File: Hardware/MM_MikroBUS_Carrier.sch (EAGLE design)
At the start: 52 parts, among them J15 MICROMOD-2222-C, J2 QWIIC_RIGHT_ANGLE, J5 Vertical Qwiic Connector, J7 MIKROBUS_SMD_BLACK1, J9 CORTEX_JTAG_DEBUG_MINIMUM_PTH, U1 MCP73831, U2 AP7361C-33FGEUDFN-8

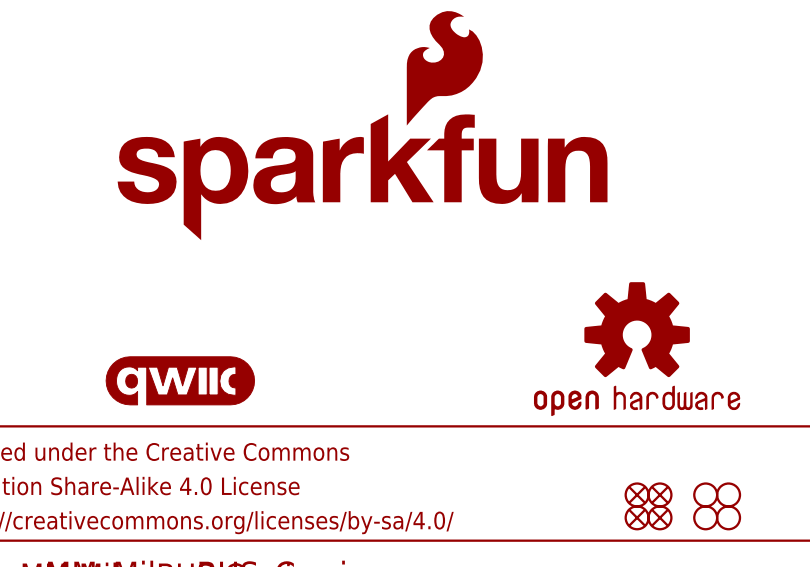
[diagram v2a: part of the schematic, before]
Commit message: Design review updates:
* Put mikroBUS pin labels into the table
* Add y-measure for mikroBUS socket
* Add mikroBUS logo to library and to the back of the board
* Add GND vias
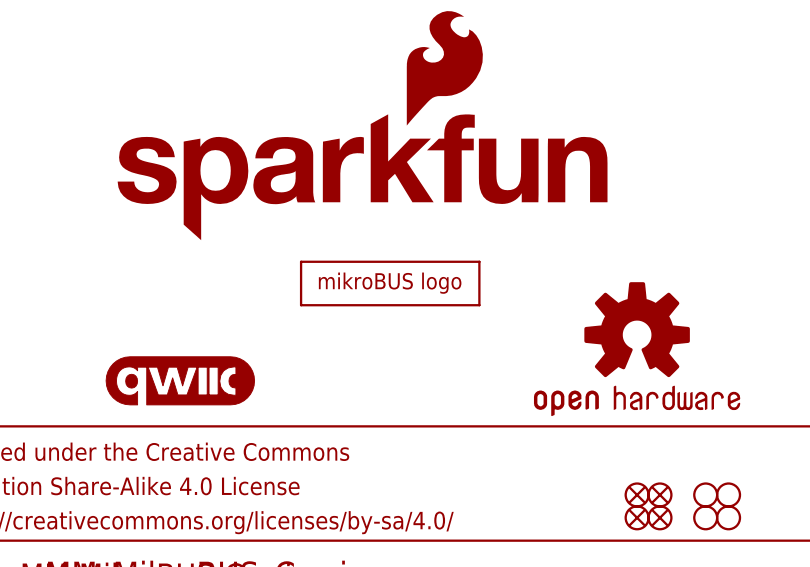
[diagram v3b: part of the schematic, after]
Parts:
- added U$7: MIKROBUS_LOGO, mikroBUS_SMD_BLACK:MIKROBUS_LOGO
- SWDCK, SWDIO: value TEST-POINT3 -> TEST-POINTTP_15TH_THRU; device SparkFun-Connectors:TEST-POINT3 -> SparkFun-Connectors:TEST-POINTTP_15TH_THRU
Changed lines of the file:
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@@
 <grid distance="0.1" unitdist="inch" unit="inch" style="lines" multiple="1" display="no" altdistance="0.01" altunitdist="inch" altunit="inch"/>
 <layers>
-<layer number="1" name="Top" color="4" fill="1" visible="no" active="no"/>
-<layer number="2" name="Route2" color="1" fill="3" visible="no" active="no"/>
-<layer number="3" name="Route3" color="4" fill="3" visible="no" active="no"/>
-<layer number="4" name="Route4" color="1" fill="4" visible="no" active="no"/>
-<layer number="5" name="Route5" color="4" fill="4" visible="no" active="no"/>
-<layer number="6" name="Route6" color="1" fill="8" visible="no" active="no"/>
-<layer number="7" name="Route7" color="4" fill="8" visible="no" active="no"/>
-<layer number="8" name="Route8" color="1" fill="2" visible="no" active="no"/>
-<layer number="9" name="Route9" color="4" fill="2" visible="no" active="no"/>
-<layer number="10" name="Route10" color="1" fill="7" visible="no" active="no"/>
-<layer number="11" name="Route11" color="4" fill="7" visible="no" active="no"/>
-<layer number="12" name="Route12" color="1" fill="5" visible="no" active="no"/>
-<layer number="13" name="Route13" color="4" fill="5" visible="no" active="no"/>
-<layer number="14" name="Route14" color="1" fill="6" visible="no" active="no"/>
-<layer number="15" name="Route15" color="4" fill="6" visible="no" active="no"/>
-<layer number="16" name="Bottom" color="1" fill="1" visible="no" active="no"/>
-<layer number="17" name="Pads" color="2" fill="1" visible="no" active="no"/>
-<layer number="18" name="Vias" color="2" fill="1" visible="no" active="no"/>
-<layer number="19" name="Unrouted" color="6" fill="1" visible="no" active="no"/>
-<layer number="20" name="Dimension" color="24" fill="1" visible="no" active="no"/>
-<layer number="21" name="tPlace" color="16" fill="1" visible="no" active="no"/>
-<layer number="22" name="bPlace" color="14" fill="1" visible="no" active="no"/>
-<layer number="23" name="tOrigins" color="15" fill="1" visible="no" active="no"/>
-<layer number="24" name="bOrigins" color="15" fill="1" visible="no" active="no"/>
-<layer number="25" name="tNames" color="7" fill="1" visible="no" active="no"/>
-<layer number="26" name="bNames" color="7" fill="1" visible="no" active="no"/>
-<layer number="27" name="tValues" color="7" fill="1" visible="no" active="no"/>
-<layer number="28" name="bValues" color="7" fill="1" visible="no" active="no"/>
+<layer number="1" name="Top" color="4" fill="1" visible="yes" active="no"/>
+<layer number="2" name="Route2" color="1" fill="3" visible="yes" active="no"/>
+<layer number="3" name="Route3" color="4" fill="3" visible="yes" active="no"/>
+<layer number="4" name="Route4" color="1" fill="4" visible="yes" active="no"/>
+<layer number="5" name="Route5" color="4" fill="4" visible="yes" active="no"/>
+<layer number="6" name="Route6" color="1" fill="8" visible="yes" active="no"/>
+<layer number="7" name="Route7" color="4" fill="8" visible="yes" active="no"/>
+<layer number="8" name="Route8" color="1" fill="2" visible="yes" active="no"/>
+<layer number="9" name="Route9" color="4" fill="2" visible="yes" active="no"/>
+<layer number="10" name="Route10" color="1" fill="7" visible="yes" active="no"/>
+<layer number="11" name="Route11" color="4" fill="7" visible="yes" active="no"/>
+<layer number="12" name="Route12" color="1" fill="5" visible="yes" active="no"/>
+<layer number="13" name="Route13" color="4" fill="5" visible="yes" active="no"/>
+<layer number="14" name="Route14" color="1" fill="6" visible="yes" active="no"/>
+<layer number="15" name="Route15" color="4" fill="6" visible="yes" active="no"/>
+<layer number="16" name="Bottom" color="1" fill="1" visible="yes" active="no"/>
+<layer number="17" name="Pads" color="2" fill="1" visible="yes" active="no"/>
+<layer number="18" name="Vias" color="2" fill="1" visible="yes" active="no"/>
+<layer number="19" name="Unrouted" color="6" fill="1" visible="yes" active="no"/>
+<layer number="20" name="Dimension" color="24" fill="1" visible="yes" active="no"/>
+<layer number="21" name="tPlace" color="16" fill="1" visible="yes" active="no"/>
+<layer number="22" name="bPlace" color="14" fill="1" visible="yes" active="no"/>
+<layer number="23" name="tOrigins" color="15" fill="1" visible="yes" active="no"/>
+<layer number="24" name="bOrigins" color="15" fill="1" visible="yes" active="no"/>
+<layer number="25" name="tNames" color="7" fill="1" visible="yes" active="no"/>
+<layer number="26" name="bNames" color="7" fill="1" visible="yes" active="no"/>
+<layer number="27" name="tValues" color="7" fill="1" visible="yes" active="no"/>
+<layer number="28" name="bValues" color="7" fill="1" visible="yes" active="no"/>
 <layer number="29" name="tStop" color="7" fill="3" visible="no" active="no"/>
 <layer number="30" name="bStop" color="7" fill="6" visible="no" active="no"/>
@@
 <layer number="35" name="tGlue" color="7" fill="4" visible="no" active="no"/>
 <layer number="36" name="bGlue" color="7" fill="5" visible="no" active="no"/>
-<layer number="37" name="tTest" color="7" fill="1" visible="no" active="no"/>
-<layer number="38" name="bTest" color="7" fill="1" visible="no" active="no"/>
+<layer number="37" name="tTest" color="7" fill="1" visible="yes" active="no"/>
+<layer number="38" name="bTest" color="7" fill="1" visible="yes" active="no"/>
 <layer number="39" name="tKeepout" color="4" fill="11" visible="no" active="no"/>
 <layer number="40" name="bKeepout" color="1" fill="11" visible="no" active="no"/>
@@
 <layer number="44" name="Drills" color="7" fill="1" visible="no" active="no"/>
 <layer number="45" name="Holes" color="7" fill="1" visible="no" active="no"/>
-<layer number="46" name="Milling" color="3" fill="1" visible="no" active="no"/>
-<layer number="47" name="Measures" color="7" fill="1" visible="no" active="no"/>
-<layer number="48" name="Document" color="7" fill="1" visible="no" active="no"/>
-<layer number="49" name="Reference" color="7" fill="1" visible="no" active="no"/>
-<layer number="50" name="dxf" color="7" fill="1" visible="no" active="no"/>
-<layer number="51" name="tDocu" color="6" fill="1" visible="no" active="no"/>
-<layer number="52" name="bDocu" color="7" fill="1" visible="no" active="no"/>
-<layer number="53" name="tGND_GNDA" color="7" fill="9" visible="no" active="no"/>
-<layer number="54" name="bGND_GNDA" color="1" fill="9" visible="no" active="no"/>
-<layer number="56" name="wert" color="7" fill="1" visible="no" active="no"/>
-<layer number="57" name="tCAD" color="7" fill="1" visible="no" active="no"/>
-<layer number="58" name="bCAD" color="7" fill="1" visible="no" active="no"/>
-<layer number="59" name="tCarbon" color="7" fill="1" visible="no" active="no"/>
-<layer number="60" name="bCarbon" color="7" fill="1" visible="no" active="no"/>
+<layer number="46" name="Milling" color="3" fill="1" visible="yes" active="no"/>
+<layer number="47" name="Measures" color="7" fill="1" visible="yes" active="no"/>
+<layer number="48" name="Document" color="7" fill="1" visible="yes" active="no"/>
+<layer number="49" name="Reference" color="7" fill="1" visible="yes" active="no"/>
+<layer number="50" name="dxf" color="7" fill="1" visible="yes" active="no"/>
+<layer number="51" name="tDocu" color="6" fill="1" visible="yes" active="no"/>
+<layer number="52" name="bDocu" color="7" fill="1" visible="yes" active="no"/>
+<layer number="53" name="tGND_GNDA" color="7" fill="9" visible="yes" active="no"/>
+<layer number="54" name="bGND_GNDA" color="1" fill="9" visible="yes" active="no"/>
+<layer number="56" name="wert" color="7" fill="1" visible="yes" active="no"/>
+<layer number="57" name="tCAD" color="7" fill="1" visible="yes" active="no"/>
+<layer number="58" name="bCAD" color="7" fill="1" visible="yes" active="no"/>
+<layer number="59" name="tCarbon" color="7" fill="1" visible="yes" active="no"/>
+<layer number="60" name="bCarbon" color="7" fill="1" visible="yes" active="no"/>
 <layer number="88" name="SimResults" color="9" fill="1" visible="yes" active="yes"/>
 <layer number="89" name="SimProbes" color="9" fill="1" visible="yes" active="yes"/>
@@
 <part name="GND13" library="SparkFun-PowerSymbols" deviceset="GND" device=""/>
 <part name="SUPPLY20" library="SparkFun-PowerSymbols" deviceset="3.3V" device=""/>
-<part name="SWDCK" library="SparkFun-Connectors" deviceset="TEST-POINT" device="3"/>
-<part name="SWDIO" library="SparkFun-Connectors" deviceset="TEST-POINT" device="3"/>
+<part name="SWDCK" library="SparkFun-Connectors" deviceset="TEST-POINT" device="TP_15TH_THRU" value="TEST-POINTTP_15TH_THRU"/>
+<part name="SWDIO" library="SparkFun-Connectors" deviceset="TEST-POINT" device="TP_15TH_THRU" value="TEST-POINTTP_15TH_THRU"/>
+<part name="U$7" library="mikroBUS_SMD_BLACK" deviceset="MIKROBUS_LOGO" device=""/>
 </parts>
 <sheets>
@@
 <attribute name="NAME" x="158.242" y="132.08" size="1.778" layer="95" font="vector" rot="R270"/>
 </instance>
+<instance part="U$7" gate="G$1" x="383.54" y="50.8" smashed="yes"/>
 </instances>
 <busses>
